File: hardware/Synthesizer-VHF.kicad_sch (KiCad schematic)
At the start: 85 parts, among them J1 Screw_Terminal_01x02, J2 Scope, J4 USB-C 2.0 16P, J5 REF_IN, J6 Scope, J7 RFOUTA, J8 Header 1x3, J9 RFOUTB, U1 LM7805A, U2 FT231XQ, U3 ATtiny1616-M, U4 ADF4351, U7 ADP150AUJZ-3.3-R7, U8 ADP150AUJZ-3.3-R7, X1 HCI 8122S-25NQ33FTL

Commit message: diecast-2x2: USB entry filter - VBUS C-L-C (1u+100p / BLM18KG601SN1D / 1u+100p), DLW21SN900SQ2L CMC on D+/D-
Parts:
- added C40, C42: 1u, Capacitor_SMD:C_0402_1005Metric, symbol Device:C
- added C41, C43: 100p C0G, Capacitor_SMD:C_0402_1005Metric, symbol Device:C
- added L1: DLW21SN900SQ2L, Inductor_SMD:L_CommonModeChoke_Coilank_ACM2012, symbol Device:L_Ferrite_Coupled_1423
- FB1: value FerriteBead_Small -> BLM18KG601SN1D; footprint Inductor_SMD:L_0805_2012Metric -> Inductor_SMD:L_0603_1608Metric; LCSC C1017 -> C85833
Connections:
- net 5V: now also C42.1, C43.1
- net GND: now also C40.2, C41.2, C42.2, C43.2
- net USB_DP_C: now reaches D6.1 (K), J4.A6 (D+), J4.B6 (D+)
- net USB_DP_C: now also L1.2; no longer C11.1, R13.2
- net VBUS_C: now reaches FB1.1, J4.A4 (VBUS), J4.A9 (VBUS), J4.B4 (VBUS), J4.B9 (VBUS)
- net VBUS_C: now also C40.1, C41.1
- net USB_DM_C: now reaches D2.1 (K), J4.A7 (D-), J4.B7 (D-)
- net USB_DM_C: now also L1.1; no longer C9.1, R24.2
- new net USB_DM: C9.1, L1.4, R24.2
- new net USB_DP: C11.1, L1.3, R13.2

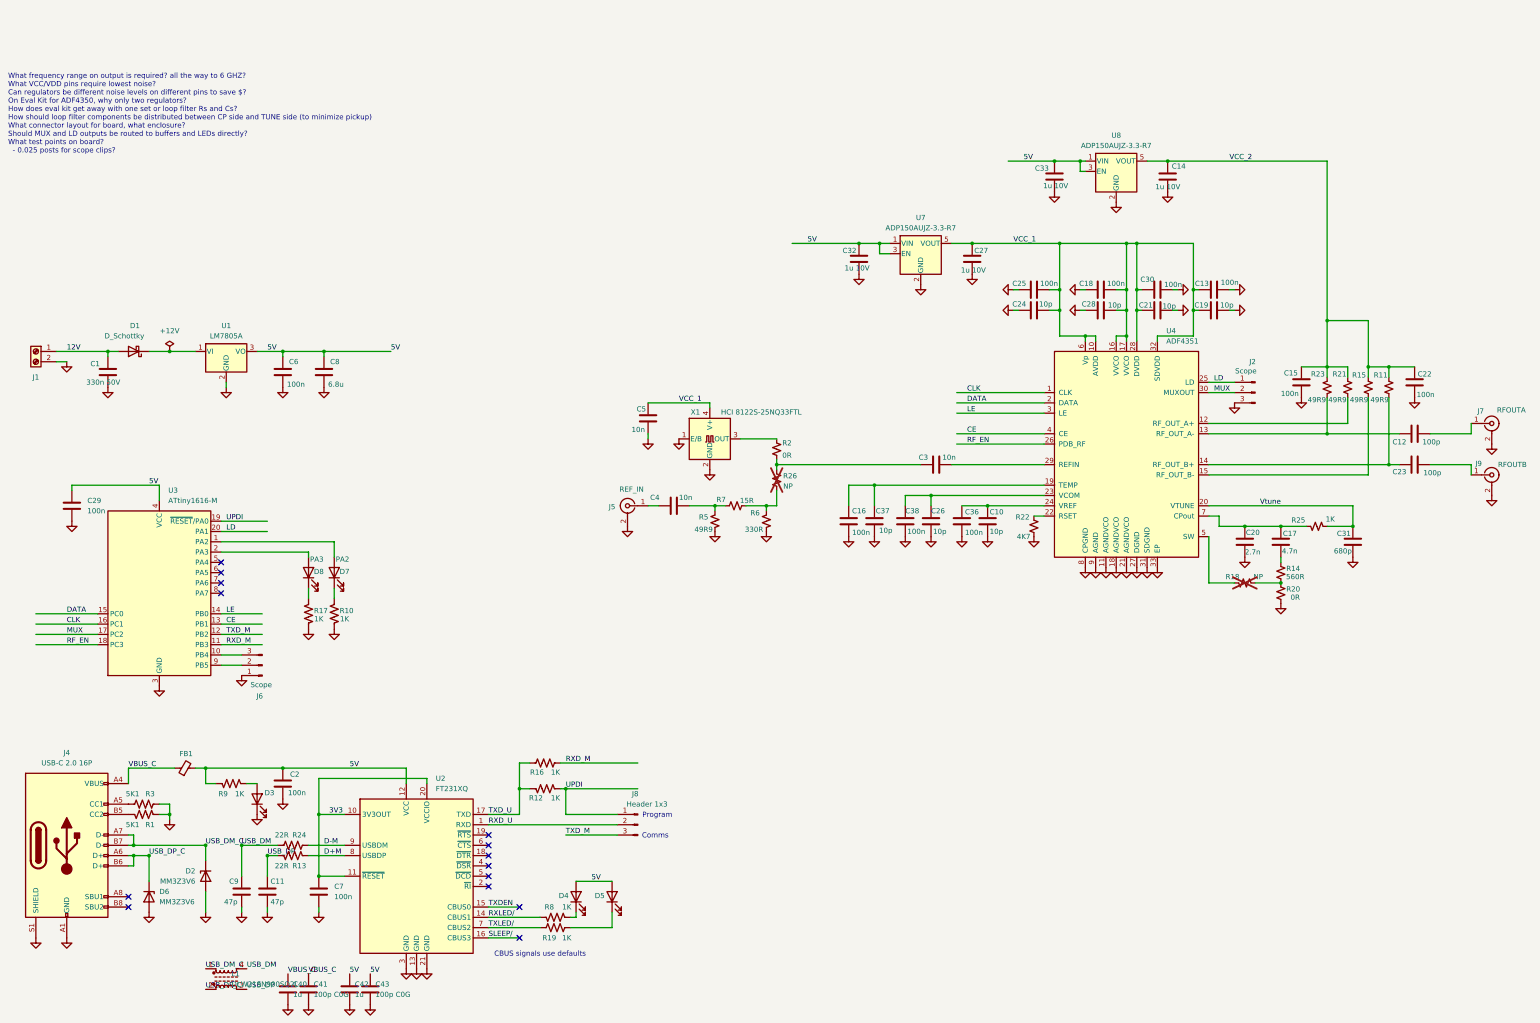
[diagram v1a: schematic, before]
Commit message: diecast-2x2: PLL loop filter R14/R18/R20/R25/C17/C20/C31 0805->0603 (schematic; run Update PCB). LCSC R14 C23204, R20 C21189, R25 C21190. Includes user's saved KiCad edits.
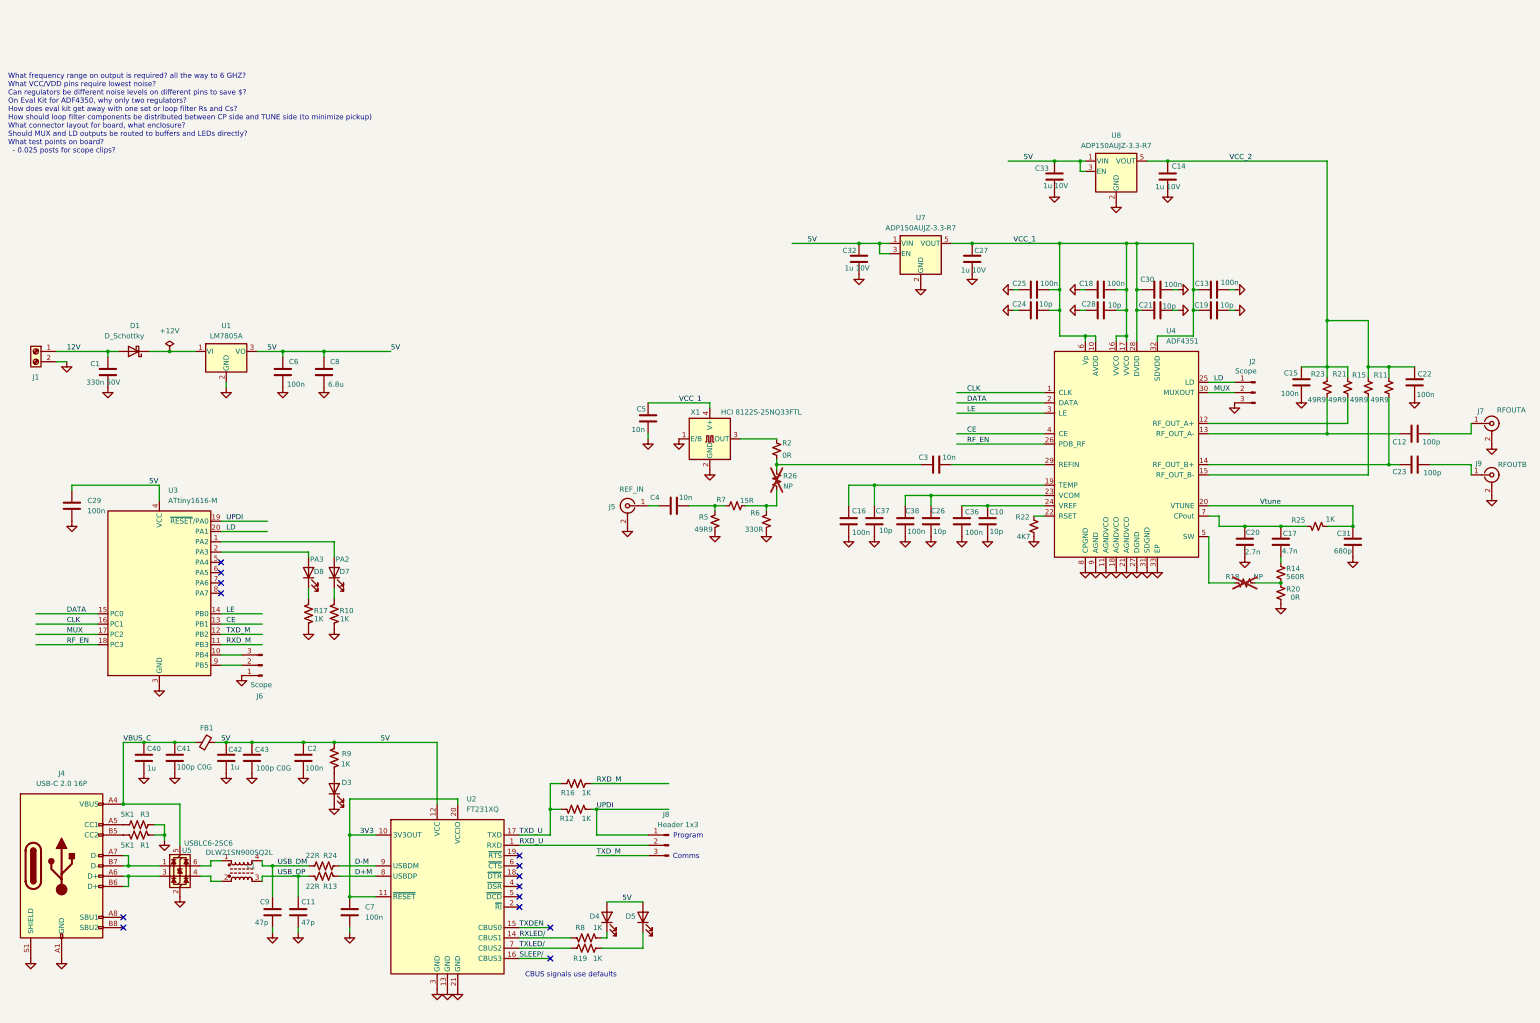
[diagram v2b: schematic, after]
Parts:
- removed D2, D6: MM3Z3V6, Diode_SMD:D_SOD-523, symbol Diode:DZ2S036X0L
- added U5: USBLC6-2SC6, Package_TO_SOT_SMD:SOT-23-6, symbol Power_Protection:USBLC6-2SC6
- C17, C20, C31: footprint Capacitor_SMD:C_0805_2012Metric -> Capacitor_SMD:C_0603_1608Metric
- J5, J7, J9: footprint Synthesizer:SMA_Amphenol_901-143_Horizontal -> Connector_Coaxial:SMA_Amphenol_901-144_Vertical
- R14: footprint Resistor_SMD:R_0805_2012Metric -> Resistor_SMD:R_0603_1608Metric; LCSC C114536 -> C23204
- R18: footprint Resistor_SMD:R_0805_2012Metric -> Resistor_SMD:R_0603_1608Metric
- R2, R26: LCSC C17168 -> C21189
- R20: footprint Resistor_SMD:R_0805_2012Metric -> Resistor_SMD:R_0603_1608Metric; LCSC C17168 -> C21189
- R25: footprint Resistor_SMD:R_0805_2012Metric -> Resistor_SMD:R_0603_1608Metric; LCSC C17513 -> C21190
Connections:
- net GND: now also U5.2 (GND)
- net VBUS_C: now also U5.5 (VBUS)
- net USB_DM_C: no longer names the net of J4.A7 (D-), J4.B7 (D-)
- net USB_DM_C: now also U5.1 (I/O1); no longer L1.1
- net USB_DP_C: no longer names the net of J4.A6 (D+), J4.B6 (D+)
- net USB_DP_C: now also U5.3 (I/O2); no longer L1.2
- new net: L1.1, U5.6 (I/O1)
- new net: L1.2, U5.4 (I/O2)
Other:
- moved on the sheet: C11, C2, C40, C41, C42, C43, C7, C9, D3, D4, D5, FB1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

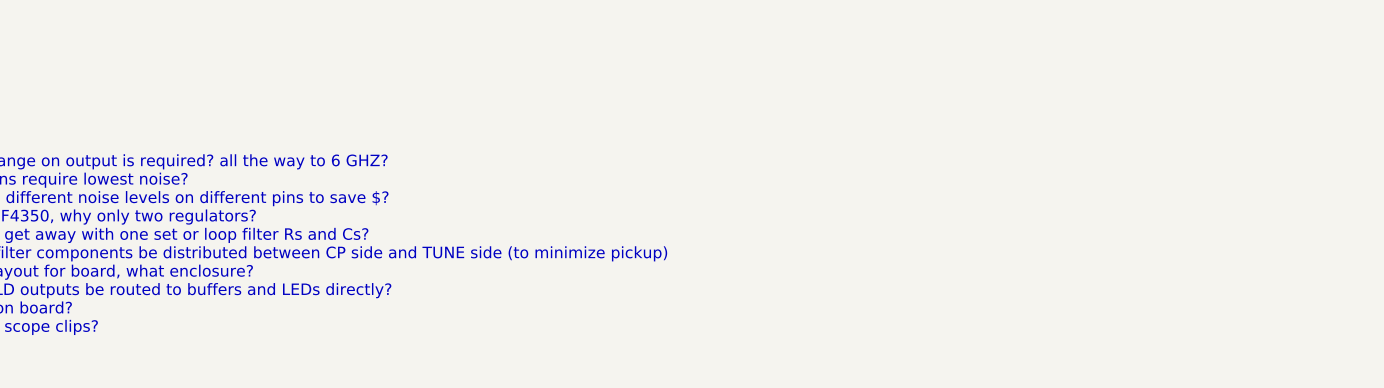
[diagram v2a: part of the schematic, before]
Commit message: diecast-2x2: add H1-H4 MountingHole_Pad symbols (GND, not in BOM) and link PCB footprints so Update PCB keeps them
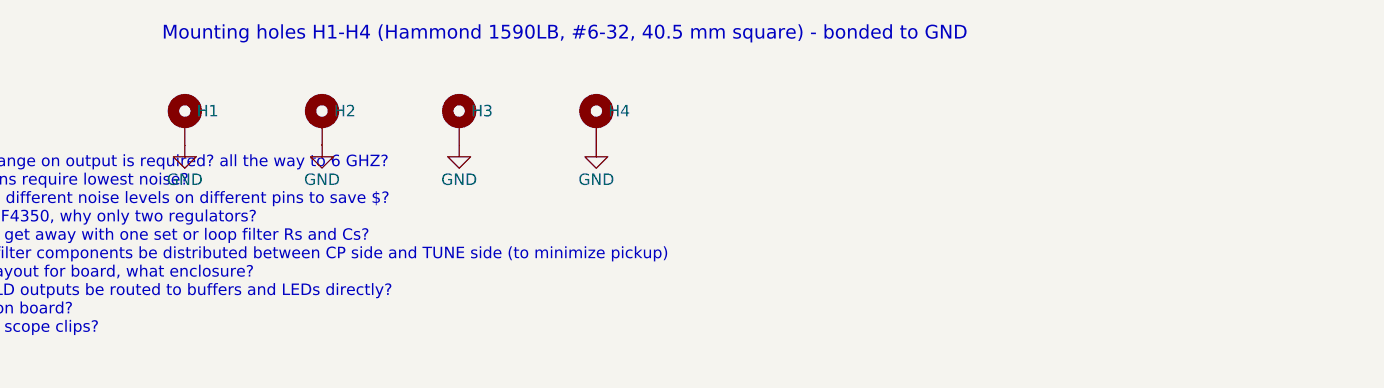
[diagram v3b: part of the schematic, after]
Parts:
- added H1, H2, H3, H4: MountingHole_6-32, Synthesizer:MountingHole_3.9mm_Pad_D5.6, symbol Mechanical:MountingHole_Pad
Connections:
- net GND: now also H1.1, H2.1, H3.1, H4.1
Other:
- note added: "Mounting holes H1-H4 (Hammond 1590LB, #6-32, 40.5 mm square) - bonded to GND"

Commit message: diecast-2x2: user layout edits (KiCad save)
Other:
- moved on the sheet: H1, H2, H3, H4

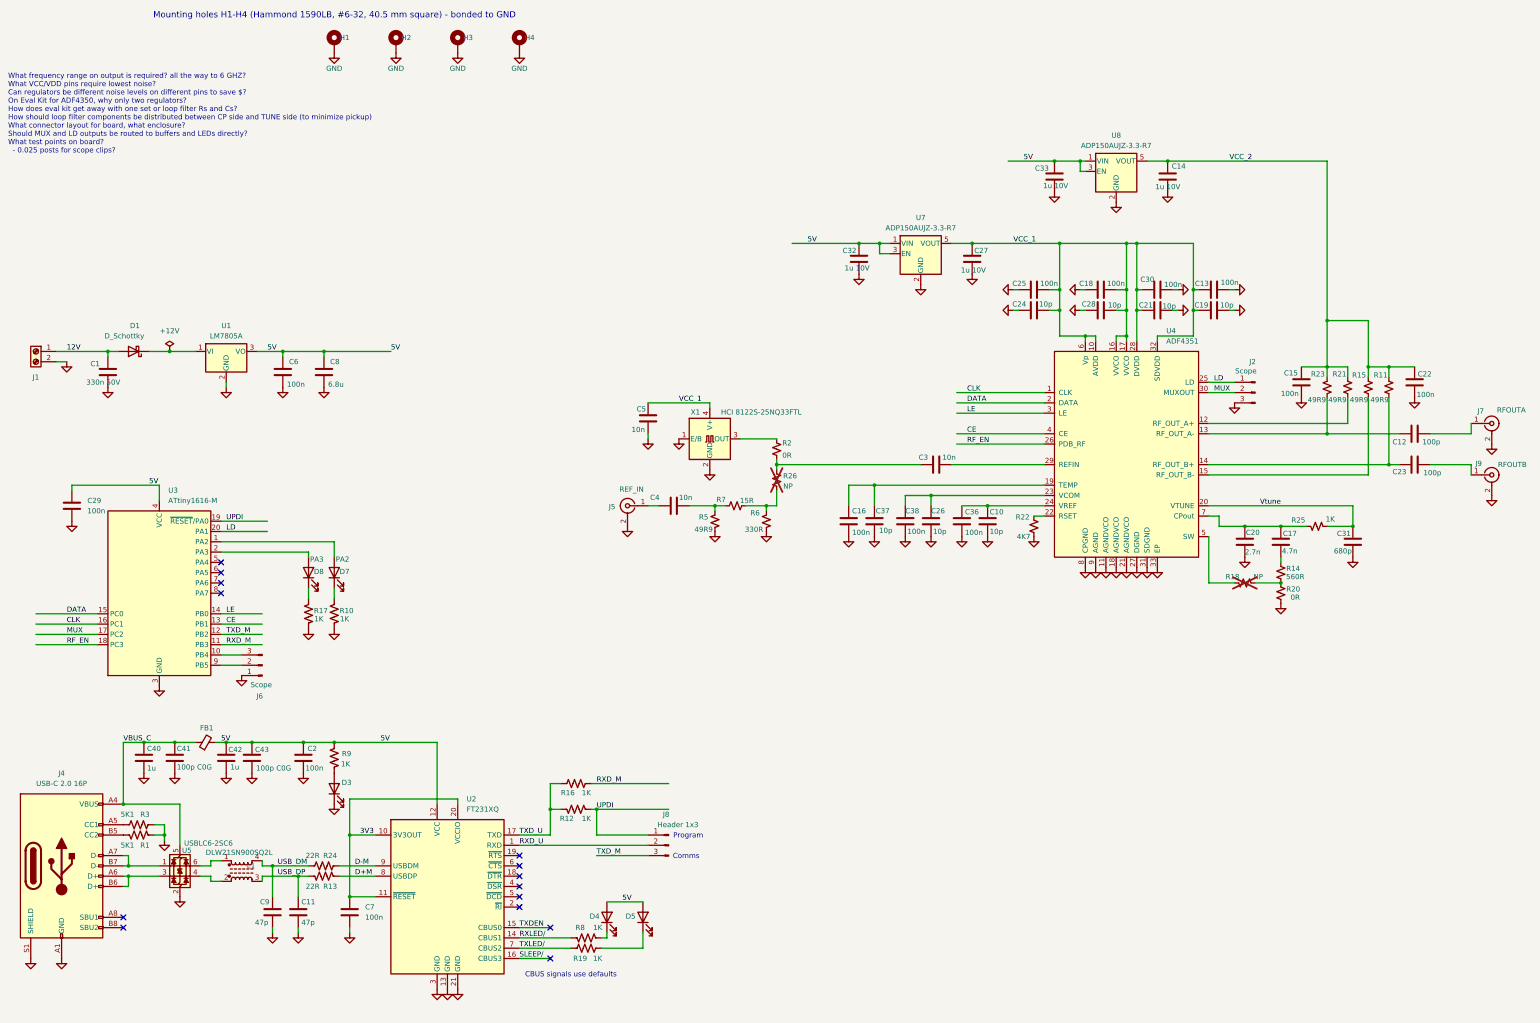
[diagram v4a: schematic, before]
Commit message: diecast-2x2: port ref out/buffer/ref-in selector and LP5907 regulators from extruded; B5819W 5V OR diodes (schematic only)
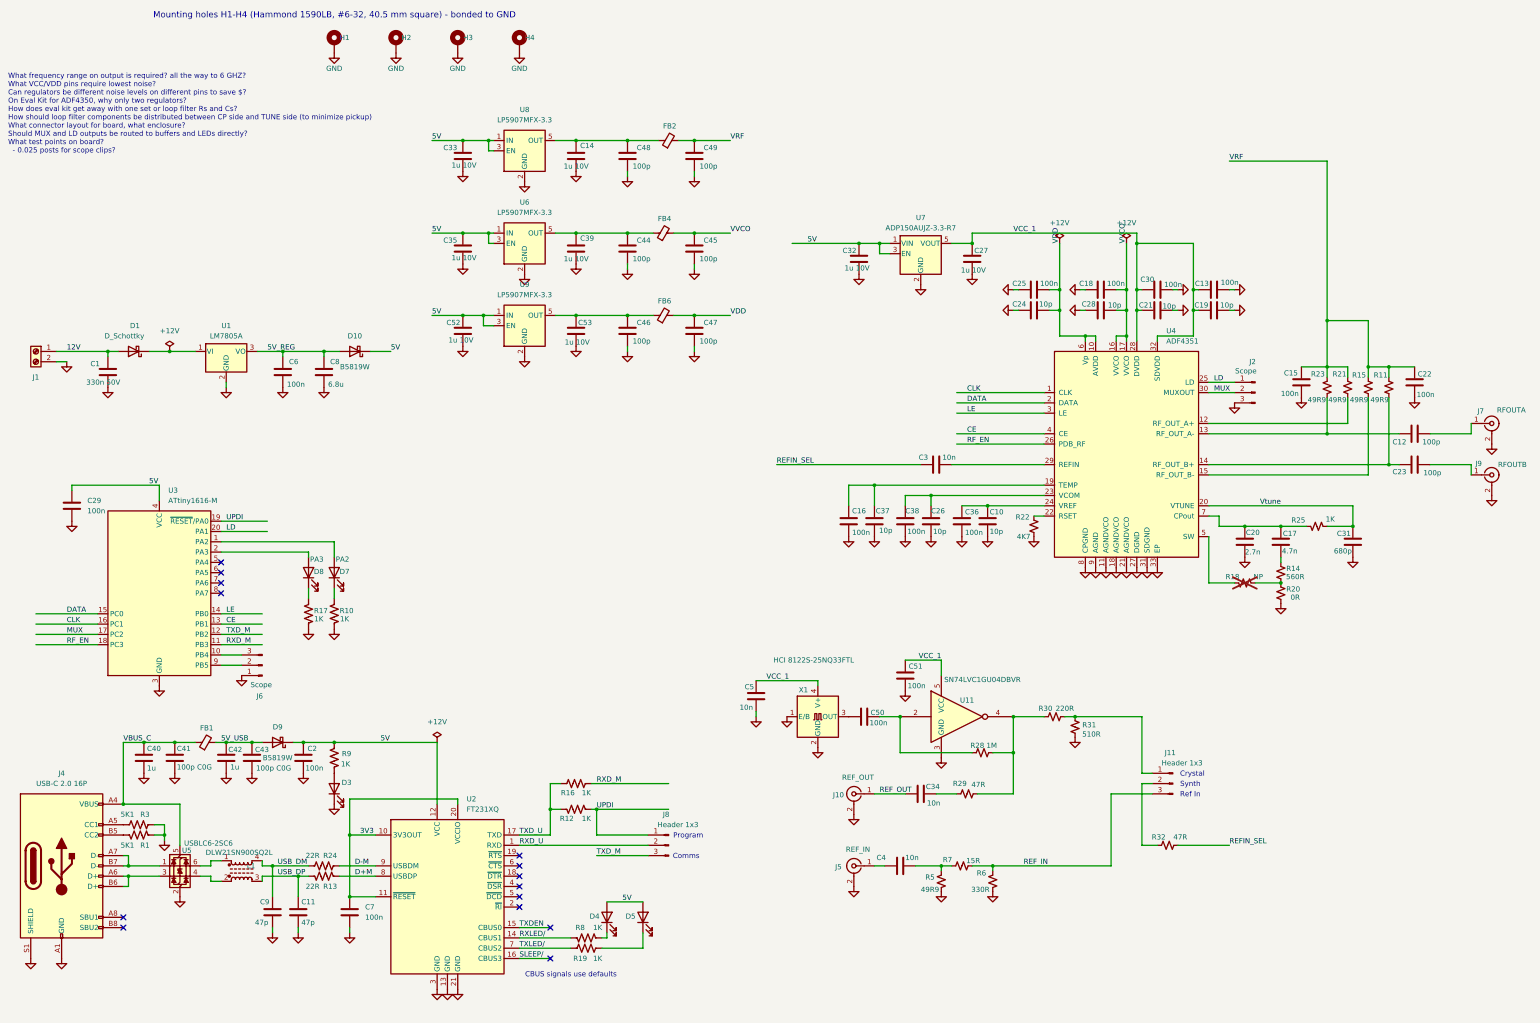
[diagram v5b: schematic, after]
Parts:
- removed R2: 0R, Resistor_SMD:R_0805_2012Metric, symbol Device:R_Small_US
- removed R26: NP, Resistor_SMD:R_0805_2012Metric, symbol Device:R_Small_US
- removed U8: ADP150AUJZ-3.3-R7, Package_TO_SOT_SMD:SOT-23-5, symbol Synthesizer:ADP150AUJZ-3.3-R7
- added C34: 10n, Synthesizer:Cap_0402, symbol Device:C
- added C35, C39, C52, C53: 1u 10V, Synthesizer:Cap_0402, symbol Device:C
- added C44, C45, C46, C47, C48, C49: 100p, Synthesizer:Cap_0402, symbol Device:C
- added C50, C51: 100n, Synthesizer:Cap_0402, symbol Device:C
- added D10, D9: B5819W, Diode_SMD:D_SOD-123, symbol Device:D_Schottky
- added FB2, FB4, FB6: FerriteBead_Small, Inductor_SMD:L_0805_2012Metric, symbol Device:FerriteBead_Small
- added J10: REF_OUT, Connector_Coaxial:SMA_Amphenol_901-144_Vertical, symbol Connector:Conn_Coaxial
- added J11: Header 1x3, Connector_PinHeader_2.54mm:PinHeader_1x03_P2.54mm_Vertical, symbol Connector:Conn_01x03_Pin
- added R28: 1M, Synthesizer:Res_0402, symbol Device:R_Small_US
- added R29, R32: 47R, Synthesizer:Res_0402, symbol Device:R_Small_US
- added R30: 220R, Synthesizer:Res_0402, symbol Device:R_Small_US
- added R31: 510R, Synthesizer:Res_0402, symbol Device:R_Small_US
- added U11: SN74LVC1GU04DBVR, Package_TO_SOT_SMD:SOT-23-5, symbol 74xGxx:74LVC1G04
- added U6, U8, U9: LP5907MFX-3.3, Package_TO_SOT_SMD:SOT-23-5, symbol Regulator_Linear:LP5907MFX-3.3
- J5: MPN (none) -> 142-0701-801
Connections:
- net 5V: now also C35.1, C52.1, D10.1 (K), D9.1 (K), U6.1 (IN), U6.3 (EN), U8.1 (IN), U8.3 (EN), U9.1 (IN), U9.3 (EN); no longer C42.1, C43.1, C6.1, C8.1, FB1.2, U1.3 (VO)
- net GND: now also C35.2, C39.2, C44.2, C45.2, C46.2, C47.2, C48.2, C49.2, C51.1, C52.2, C53.2, J10.2 (Ext), R31.2, U11.3 (GND), U6.2 (GND), U8.2 (GND), U9.2 (GND)
- net VCC_1: now also C51.2, U11.5 (VCC); no longer C18.1, C24.1, C25.1, C28.2, U4.10 (AVDD), U4.16 (VVCO), U4.17 (VVCO), U4.6 (Vp)
- net at X1.3 (OUT): now also C50.1
- net REF_IN: now reaches R6.1, R7.2
- net REF_IN: now also J11.3 (Pin_3)
- net REFIN_SEL: now reaches C3.2
- net REFIN_SEL: now also R32.2
- net VCC_2 renamed VRF
- net VRF: now also C49.1, FB2.2; no longer C14.1
- new net: C46.1, C53.1, FB6.1, U9.5 (OUT)
- new net: C14.1, C48.1, FB2.1, U8.5 (OUT)
- new net: C34.1, R29.1
- new net: J11.1 (Pin_1), R30.2, R31.1
- new net: C39.1, C44.1, FB4.1, U6.5 (OUT)
- new net: C50.2, R28.1, U11.2
- new net: R28.2, R29.2, R30.1, U11.4
- new net: J11.2 (Pin_2), R32.1
- new net 5V_REG: C6.1, C8.1, D10.2 (A), U1.3 (VO)
- new net 5V_USB: C42.1, C43.1, D9.2 (A), FB1.2
- new net REF_OUT: C34.2, J10.1 (In)
- new net VDD: C24.1, C25.1, C47.1, FB6.2, U4.10 (AVDD), U4.6 (Vp)
- new net VVCO: C18.1, C28.2, C45.1, FB4.2, U4.16 (VVCO), U4.17 (VVCO)
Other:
- note added: "Crystal"
- note added: "Ref In"
- note added: "Synth"
